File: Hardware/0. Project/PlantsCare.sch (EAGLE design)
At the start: 22 parts, among them J1 ICSP, Q1 32.768 kHz, U1 MSP430FR4133

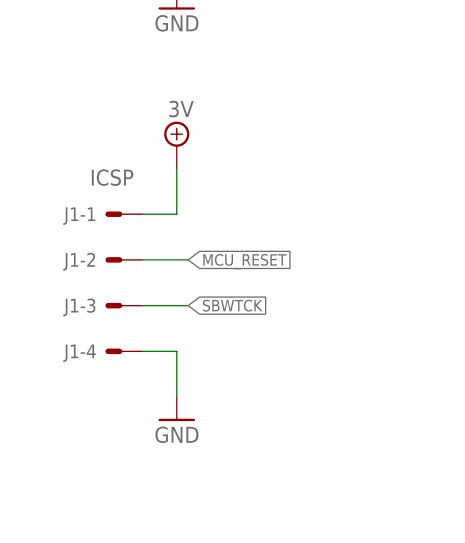
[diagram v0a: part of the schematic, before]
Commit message: BOM .csv file formatted as GitHub needed
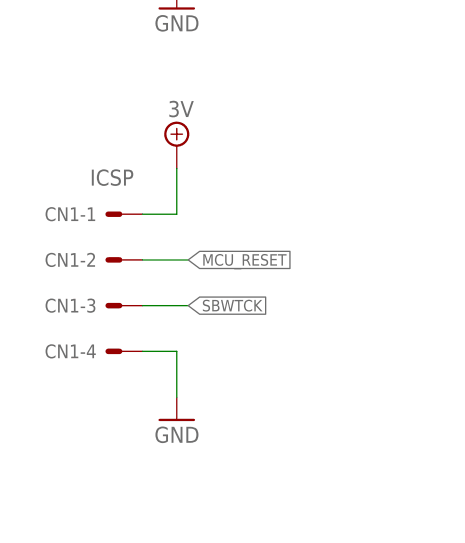
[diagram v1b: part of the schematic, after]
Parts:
- renumbered J1 to CN1
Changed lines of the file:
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@@
 <part name="GND12" library="supply1" library_urn="urn:adsk.eagle:library:371" deviceset="GND" device=""/>
 <part name="Q1" library="crystal-geyer_V1_0" library_urn="urn:adsk.eagle:library:203" deviceset="KX-327" device="-NHF" package3d_urn="urn:adsk.eagle:package:11937/1" value="32.768 kHz"/>
-<part name="J1" library="con-molex" library_urn="urn:adsk.eagle:library:165" deviceset="22-?-04" device="05-7048" package3d_urn="urn:adsk.eagle:package:8078648/1" value="ICSP"/>
+<part name="CN1" library="con-molex" library_urn="urn:adsk.eagle:library:165" deviceset="22-?-04" device="05-7048" package3d_urn="urn:adsk.eagle:package:8078648/1" value="ICSP"/>
 <part name="SUPPLY2" library="supply2" library_urn="urn:adsk.eagle:library:372" deviceset="+4.1V" device="" value="3V"/>
 <part name="GND1" library="supply1" library_urn="urn:adsk.eagle:library:371" deviceset="GND" device=""/>
@@
 <attribute name="VALUE" x="187.96" y="143.51" size="1.778" layer="96"/>
 </instance>
-<instance part="J1" gate="-1" x="15.24" y="34.29" smashed="yes" rot="MR0">
+<instance part="CN1" gate="-1" x="15.24" y="34.29" smashed="yes" rot="MR0">
 <attribute name="NAME" x="12.7" y="33.528" size="1.524" layer="95" rot="MR0"/>
 <attribute name="VALUE" x="11.938" y="39.243" size="1.778" layer="96" rot="MR180"/>
 </instance>
-<instance part="J1" gate="-2" x="15.24" y="29.21" smashed="yes" rot="MR0">
+<instance part="CN1" gate="-2" x="15.24" y="29.21" smashed="yes" rot="MR0">
 <attribute name="NAME" x="12.7" y="28.448" size="1.524" layer="95" rot="MR0"/>
 </instance>
-<instance part="J1" gate="-3" x="15.24" y="24.13" smashed="yes" rot="MR0">
+<instance part="CN1" gate="-3" x="15.24" y="24.13" smashed="yes" rot="MR0">
 <attribute name="NAME" x="12.7" y="23.368" size="1.524" layer="95" rot="MR0"/>
 </instance>
-<instance part="J1" gate="-4" x="15.24" y="19.05" smashed="yes" rot="MR0">
+<instance part="CN1" gate="-4" x="15.24" y="19.05" smashed="yes" rot="MR0">
 <attribute name="NAME" x="12.7" y="18.288" size="1.524" layer="95" rot="MR0"/>
 </instance>
@@
 </segment>
 <segment>
-<pinref part="J1" gate="-4" pin="S"/>
+<pinref part="CN1" gate="-4" pin="S"/>
 <wire x1="17.78" y1="19.05" x2="21.59" y2="19.05" width="0.1524" layer="91"/>
 <pinref part="GND1" gate="1" pin="GND"/>
@@
 </segment>
 <segment>
-<pinref part="J1" gate="-1" pin="S"/>
+<pinref part="CN1" gate="-1" pin="S"/>
 <wire x1="17.78" y1="34.29" x2="21.59" y2="34.29" width="0.1524" layer="91"/>
 <pinref part="SUPPLY2" gate="P" pin="+4.1V"/>
@@
 </segment>
 <segment>
-<pinref part="J1" gate="-2" pin="S"/>
+<pinref part="CN1" gate="-2" pin="S"/>
 <wire x1="17.78" y1="29.21" x2="22.86" y2="29.21" width="0.1524" layer="91"/>
 <label x="22.86" y="29.21" size="1.27" layer="95" ratio="5" rot="MR180" xref="yes"/>
@@
 </segment>
 <segment>
-<pinref part="J1" gate="-3" pin="S"/>
+<pinref part="CN1" gate="-3" pin="S"/>
 <wire x1="17.78" y1="24.13" x2="22.86" y2="24.13" width="0.1524" layer="91"/>
 <label x="22.86" y="24.13" size="1.27" layer="95" ratio="5" rot="MR180" xref="yes"/>

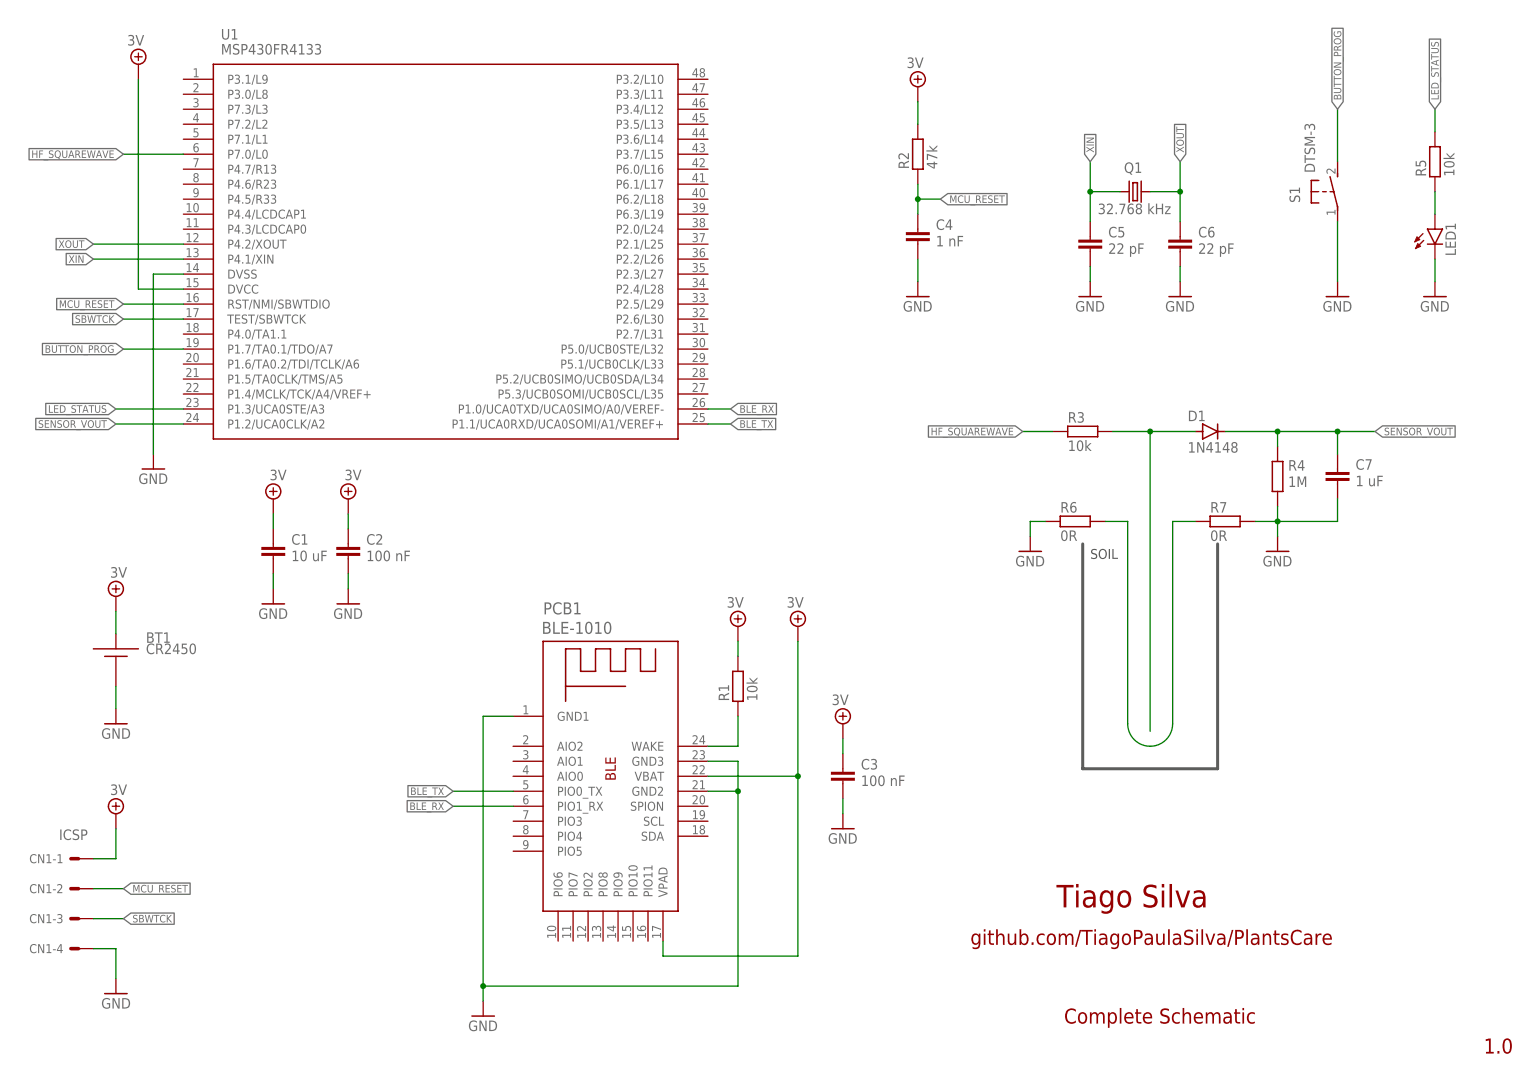
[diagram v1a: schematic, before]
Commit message: Schematic organization improved
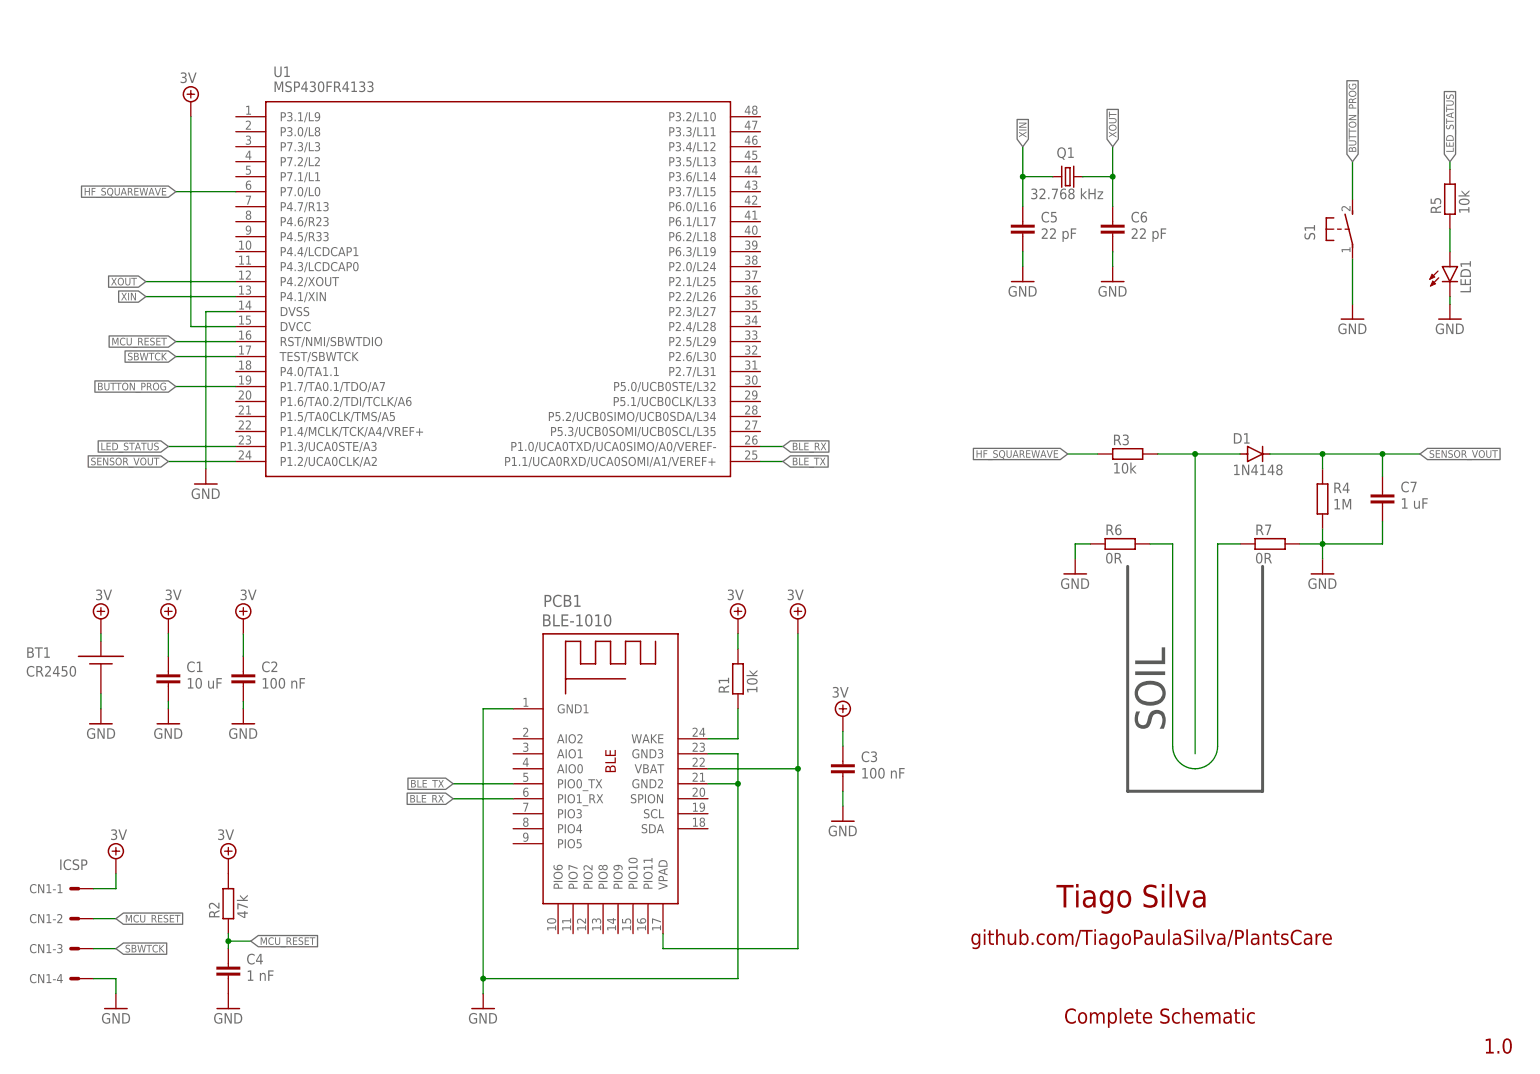
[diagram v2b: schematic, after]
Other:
- note added: "BLUETOOTH LOW ENERGY MODULE"
- note added: "CAPACITIVE SOIL MOISTURE SENSOR"
- note added: "IN-CIRCUIT SERIAL PROGRAMMING"
- note added: "LOW POWER OSCILLATOR"
- note added: "MICROCONTROLLER"
- note added: "POWER SUPPLY"
- note added: "USER INTERFACE"
- moved on the sheet: BT1, C1, C2, C3, C4, C5, C6, C7, CN1-1, CN1-2, CN1-3, CN1-4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

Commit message: Schematic updated to 1.2 revision
--------------------------------------------------------------------
* HF_SQUAREWAVE signal removed from P7.0 and connected to P1.4
- P1.4 has a native function thats provides a MCLK clock as OUTPUT. This way, isn't necessery manually generates a high freq. signal with another pin.
--------------------------------------------------------------------
* BLE_WAKE signal added to P1.5
- This will allows the MCU wake-up the BLE with a single low level pulse.
--------------------------------------------------------------------
* BLE_STATUS signal added to P1.6.
- This will allows the MCU knows when BLE is connected or not.
--------------------------------------------------------------------
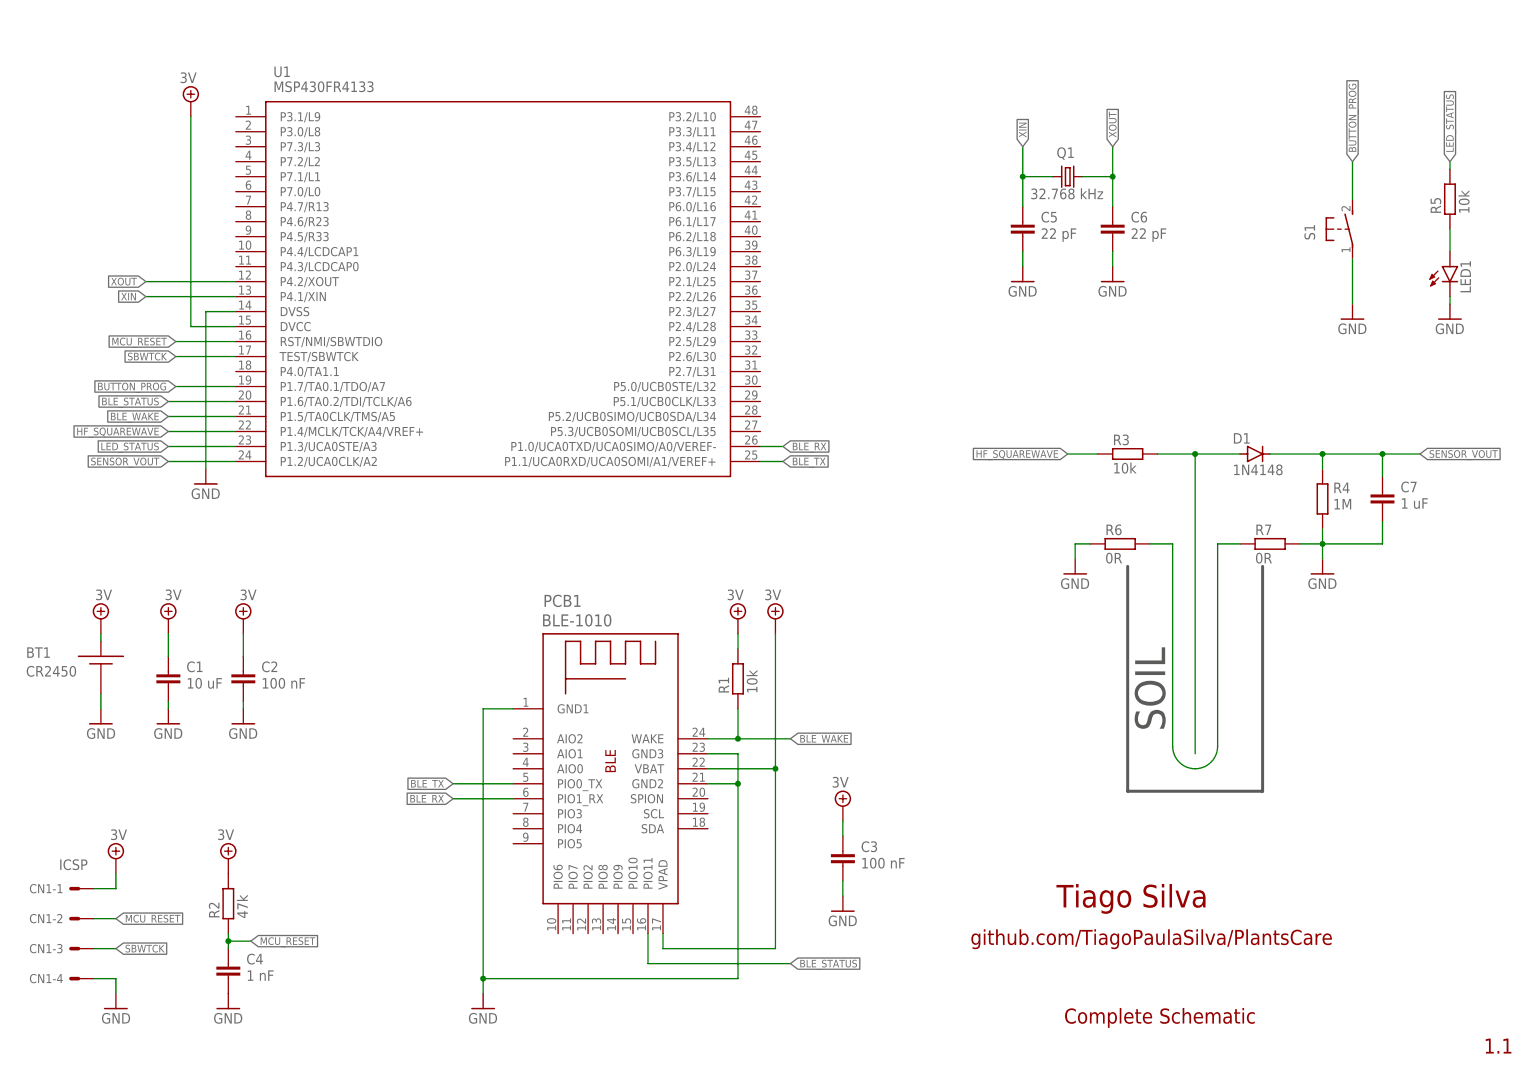
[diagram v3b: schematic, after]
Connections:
- removed net BLE_WAKE1: PCB1.WAKE, R1.2
- new net BLE_STATUS: PCB1.PIO11, U1.P1.6/TA0.2/TDI/TCLK/A6
- new net BLE_WAKE: PCB1.WAKE, R1.2, U1.P1.5/TA0CLK/TMS/A5
- net HF_SQUAREWAVE: now also U1.P1.4/MCLK/TCK/A4/VREF+; no longer U1.P7.0/L0
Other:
- note added: "1.1"
- note removed: "1.0"
- moved on the sheet: C3
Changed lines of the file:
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@@
 <rectangle x1="193.04" y1="45.72" x2="215.9" y2="83.82" layer="208"/>
 <text x="199.39" y="55.88" size="5.08" layer="97" distance="40" rot="R90">SOIL</text>
-<text x="253.365" y="1.27" size="2.54" layer="94" ratio="5">1.0</text>
+<text x="253.365" y="1.27" size="2.54" layer="94" ratio="5">1.1</text>
 <text x="182.245" y="6.35" size="2.54" layer="94" ratio="5">Complete Schematic</text>
 <wire x1="2.54" y1="177.8" x2="2.54" y2="92.71" width="0.508" layer="152" style="longdash"/>
@@
 <attribute name="VALUE" x="81.28" y="6.35" size="1.778" layer="96"/>
 </instance>
-<instance part="SUPPLY6" gate="P" x="137.16" y="74.93" smashed="yes">
-<attribute name="VALUE" x="135.255" y="78.105" size="1.778" layer="96"/>
+<instance part="SUPPLY6" gate="P" x="133.35" y="74.93" smashed="yes">
+<attribute name="VALUE" x="131.445" y="78.105" size="1.778" layer="96"/>
 </instance>
 <instance part="SUPPLY5" gate="P" x="127" y="74.93" smashed="yes">
@@
 <attribute name="VALUE" x="38.735" y="37.465" size="1.778" layer="96"/>
 </instance>
-<instance part="C3" gate="G$1" x="144.78" y="50.8" smashed="yes">
-<attribute name="NAME" x="147.828" y="50.673" size="1.778" layer="95"/>
-<attribute name="VALUE" x="147.828" y="47.879" size="1.778" layer="96"/>
-</instance>
-<instance part="SUPPLY7" gate="P" x="144.78" y="58.42" smashed="yes">
-<attribute name="VALUE" x="142.875" y="61.595" size="1.778" layer="96"/>
-</instance>
-<instance part="GND6" gate="1" x="144.78" y="40.64" smashed="yes">
-<attribute name="VALUE" x="142.24" y="38.1" size="1.778" layer="96"/>
+<instance part="C3" gate="G$1" x="144.78" y="35.56" smashed="yes">
+<attribute name="NAME" x="147.828" y="35.433" size="1.778" layer="95"/>
+<attribute name="VALUE" x="147.828" y="32.639" size="1.778" layer="96"/>
+</instance>
+<instance part="SUPPLY7" gate="P" x="144.78" y="43.18" smashed="yes">
+<attribute name="VALUE" x="142.875" y="46.355" size="1.778" layer="96"/>
+</instance>
+<instance part="GND6" gate="1" x="144.78" y="25.4" smashed="yes">
+<attribute name="VALUE" x="142.24" y="22.86" size="1.778" layer="96"/>
 </instance>
 <instance part="GND12" gate="1" x="231.14" y="125.73" smashed="yes">
@@
 </segment>
 <segment>
-<label x="31.75" y="147.32" size="1.27" layer="95" ratio="5" rot="R180" xref="yes"/>
-<pinref part="U1" gate="G$1" pin="P7.0/L0"/>
-<wire x1="41.91" y1="147.32" x2="31.75" y2="147.32" width="0.1524" layer="91"/>
+<label x="30.48" y="106.68" size="1.27" layer="95" ratio="5" rot="R180" xref="yes"/>
+<wire x1="30.48" y1="106.68" x2="41.91" y2="106.68" width="0.1524" layer="91"/>
+<pinref part="U1" gate="G$1" pin="P1.4/MCLK/TCK/A4/VREF+"/>
 </segment>
 </net>
@@
 <pinref part="C3" gate="G$1" pin="2"/>
 <pinref part="GND6" gate="1" pin="GND"/>
-<wire x1="144.78" y1="43.18" x2="144.78" y2="45.72" width="0.1524" layer="91"/>
+<wire x1="144.78" y1="27.94" x2="144.78" y2="30.48" width="0.1524" layer="91"/>
 </segment>
 <segment>
@@
 </segment>
 </net>
-<net name="BLE_WAKE1" class="0">
+<net name="BLE_WAKE" class="0">
 <segment>
 <pinref part="PCB1" gate="G$1" pin="WAKE"/>
@@
 <wire x1="127" y1="59.69" x2="127" y2="54.61" width="0.1524" layer="91"/>
 <pinref part="R1" gate="G$1" pin="2"/>
+<wire x1="127" y1="54.61" x2="135.89" y2="54.61" width="0.1524" layer="91"/>
+<junction x="127" y="54.61"/>
+<label x="135.89" y="54.61" size="1.27" layer="95" ratio="5" xref="yes"/>
+</segment>
+<segment>
+<pinref part="U1" gate="G$1" pin="P1.5/TA0CLK/TMS/A5"/>
+<wire x1="41.91" y1="109.22" x2="30.48" y2="109.22" width="0.1524" layer="91"/>
+<label x="30.48" y="109.22" size="1.27" layer="95" ratio="5" rot="R180" xref="yes"/>
 </segment>
 </net>
@@
 <pinref part="PCB1" gate="G$1" pin="VBAT"/>
 <pinref part="SUPPLY6" gate="P" pin="+4.1V"/>
-<wire x1="121.92" y1="49.53" x2="137.16" y2="49.53" width="0.1524" layer="91"/>
-<wire x1="137.16" y1="49.53" x2="137.16" y2="72.39" width="0.1524" layer="91"/>
-<wire x1="114.3" y1="19.05" x2="137.16" y2="19.05" width="0.1524" layer="91"/>
-<wire x1="137.16" y1="19.05" x2="137.16" y2="49.53" width="0.1524" layer="91"/>
-<junction x="137.16" y="49.53"/>
+<wire x1="121.92" y1="49.53" x2="133.35" y2="49.53" width="0.1524" layer="91"/>
+<wire x1="133.35" y1="49.53" x2="133.35" y2="72.39" width="0.1524" layer="91"/>
+<wire x1="114.3" y1="19.05" x2="133.35" y2="19.05" width="0.1524" layer="91"/>
+<wire x1="133.35" y1="19.05" x2="133.35" y2="49.53" width="0.1524" layer="91"/>
+<junction x="133.35" y="49.53"/>
 <pinref part="PCB1" gate="G$1" pin="VPAD"/>
 <wire x1="114.3" y1="19.05" x2="114.3" y2="21.59" width="0.1524" layer="91"/>
@@
 <pinref part="C3" gate="G$1" pin="1"/>
 <pinref part="SUPPLY7" gate="P" pin="+4.1V"/>
-<wire x1="144.78" y1="55.88" x2="144.78" y2="53.34" width="0.1524" layer="91"/>
+<wire x1="144.78" y1="40.64" x2="144.78" y2="38.1" width="0.1524" layer="91"/>
 </segment>
 <segment>
@@
 </segment>
 </net>
+<net name="BLE_STATUS" class="0">
+<segment>
+<pinref part="PCB1" gate="G$1" pin="PIO11"/>
+<wire x1="111.76" y1="21.59" x2="111.76" y2="16.51" width="0.1524" layer="91"/>
+<wire x1="111.76" y1="16.51" x2="135.89" y2="16.51" width="0.1524" layer="91"/>
+<label x="135.89" y="16.51" size="1.27" layer="95" ratio="5" xref="yes"/>
+</segment>
+<segment>
+<pinref part="U1" gate="G$1" pin="P1.6/TA0.2/TDI/TCLK/A6"/>
+<wire x1="41.91" y1="111.76" x2="30.48" y2="111.76" width="0.1524" layer="91"/>
+<label x="30.48" y="111.76" size="1.27" layer="95" ratio="5" rot="R180" xref="yes"/>
+</segment>
+</net>
